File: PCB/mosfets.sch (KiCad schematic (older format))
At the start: 16 parts

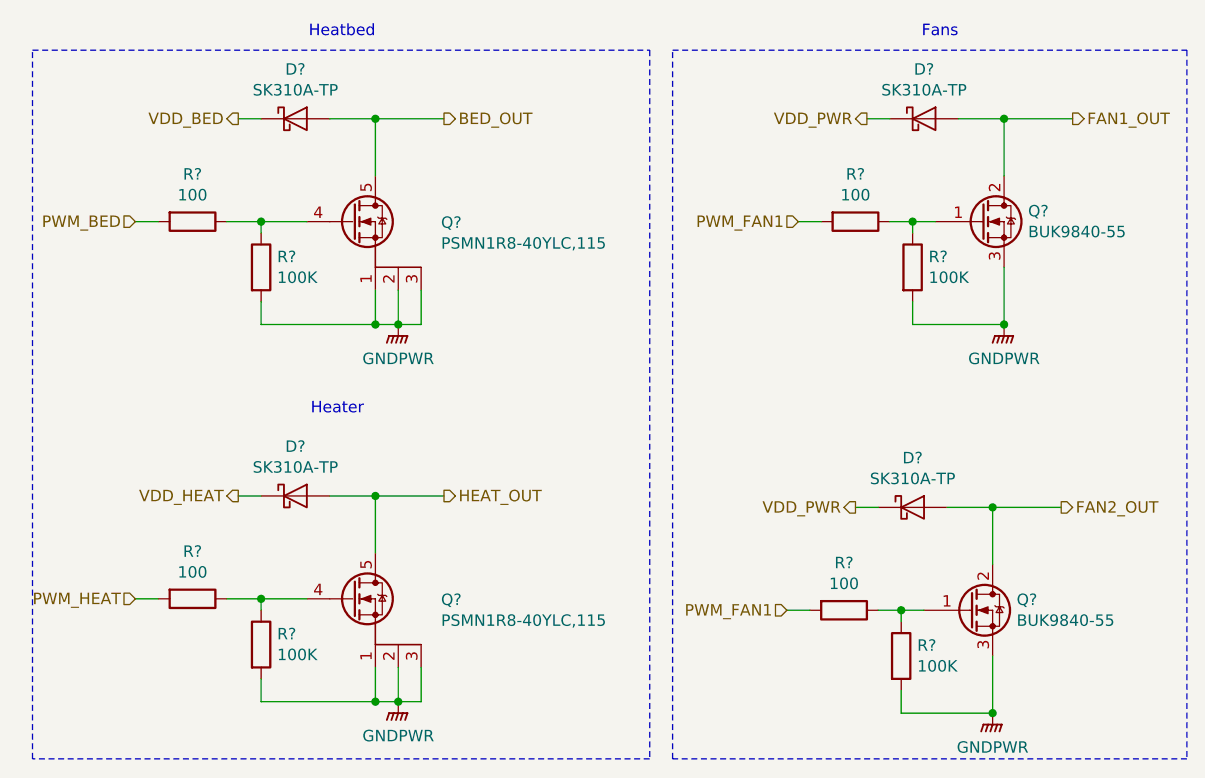
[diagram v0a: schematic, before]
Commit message: Removed some resistors for mosfets.
I don't think they are needed.
Also added some missing footprints.
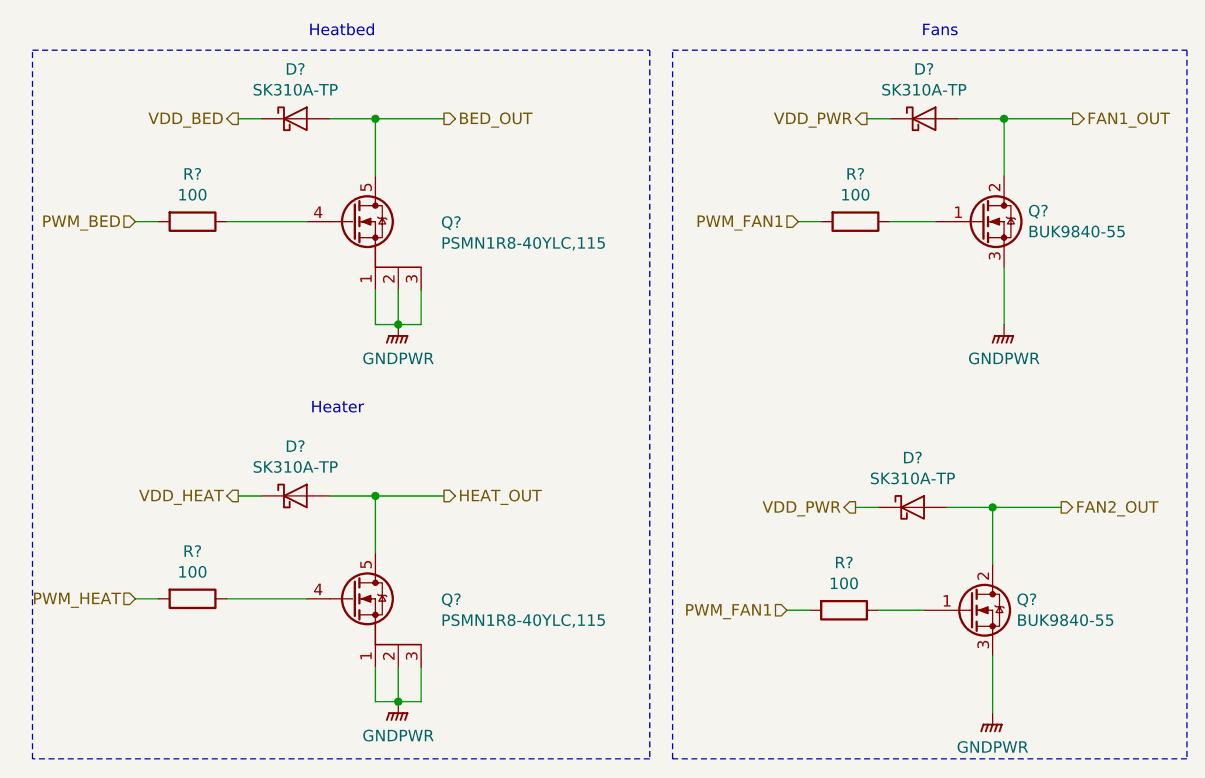
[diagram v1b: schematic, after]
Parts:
- removed R? (x4): 100K, Resistor_SMD:R_0603_1608Metric, symbol Device:R
- R? (x2): footprint (none) -> Resistor_SMD:R_0603_1608Metric
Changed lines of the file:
@@
 	2400 2600 2100 2600
 Connection ~ 2100 2600
-Wire Wire Line
-	1600 3050 1800 3050
-Wire Wire Line
-	1600 3100 1600 3050
-Connection ~ 1600 3050
-Wire Wire Line
-	1450 3050 1600 3050
-Wire Wire Line
-	1600 3400 1600 3500
-Connection ~ 2100 3500
-Wire Wire Line
-	1600 3500 2100 3500
-$Comp
-L Device:R R?
-U 1 1 5B1B03D2
-P 1600 3250
-F 0 "R?" H 1670 3296 50  0000 L CNN
-F 1 "100K" H 1670 3205 50  0000 L CNN
-F 2 "Resistor_SMD:R_0603_1608Metric" V 1530 3250 50  0001 C CNN
-F 3 "~" H 1600 3250 50  0001 C CNN
-	1    1600 3250
-	1    0    0    -1
-$EndComp
-Wire Wire Line
-	1600 1400 1800 1400
-Wire Wire Line
-	1450 1400 1600 1400
-Connection ~ 1600 1400
-Wire Wire Line
-	1600 1450 1600 1400
-Connection ~ 2100 1850
-Wire Wire Line
-	1600 1850 2100 1850
-Wire Wire Line
-	1600 1750 1600 1850
-$Comp
-L Device:R R?
-U 1 1 5B1A82F4
-P 1600 1600
-F 0 "R?" H 1670 1646 50  0000 L CNN
-F 1 "100K" H 1670 1555 50  0000 L CNN
-F 2 "Resistor_SMD:R_0603_1608Metric" V 1530 1600 50  0001 C CNN
-F 3 "~" H 1600 1600 50  0001 C CNN
-	1    1600 1600
-	1    0    0    -1
-$EndComp
 $Comp
 L remram-custom:BUK9840-55 Q?
@@
 F 0 "R?" V 3993 1400 50  0000 C CNN
 F 1 "100" V 4084 1400 50  0000 C CNN
-F 2 "" V 4130 1400 50  0001 C CNN
+F 2 "Resistor_SMD:R_0603_1608Metric" V 4130 1400 50  0001 C CNN
 F 3 "~" H 4200 1400 50  0001 C CNN
 	1    4200 1400
@@
 Wire Wire Line
 	3950 1400 4050 1400
-Wire Wire Line
-	4450 1750 4450 1850
-$Comp
-L Device:R R?
-U 1 1 5B1FCA24
-P 4450 1600
-F 0 "R?" H 4520 1646 50  0000 L CNN
-F 1 "100K" H 4520 1555 50  0000 L CNN
-F 2 "Resistor_SMD:R_0603_1608Metric" V 4380 1600 50  0001 C CNN
-F 3 "~" H 4450 1600 50  0001 C CNN
-	1    4450 1600
-	1    0    0    -1
-$EndComp
-Wire Wire Line
-	4350 1400 4450 1400
-Wire Wire Line
-	4450 1450 4450 1400
-Connection ~ 4450 1400
-Wire Wire Line
-	4450 1400 4550 1400
 $Comp
 L power:GNDPWR #PWR?
@@
 	1    0    0    -1
 $EndComp
-Wire Wire Line
-	4450 1850 4850 1850
-Connection ~ 4850 1850
 Text HLabel 5150 950  2    50   Output ~ 0
 FAN1_OUT
@@
 F 0 "R?" V 3943 3100 50  0000 C CNN
 F 1 "100" V 4034 3100 50  0000 C CNN
-F 2 "" V 4080 3100 50  0001 C CNN
+F 2 "Resistor_SMD:R_0603_1608Metric" V 4080 3100 50  0001 C CNN
 F 3 "~" H 4150 3100 50  0001 C CNN
 	1    4150 3100
@@
 Wire Wire Line
 	3900 3100 4000 3100
-Wire Wire Line
-	4400 3450 4400 3550
-$Comp
-L Device:R R?
-U 1 1 5B2008DA
-P 4400 3300
-F 0 "R?" H 4470 3346 50  0000 L CNN
-F 1 "100K" H 4470 3255 50  0000 L CNN
-F 2 "Resistor_SMD:R_0603_1608Metric" V 4330 3300 50  0001 C CNN
-F 3 "~" H 4400 3300 50  0001 C CNN
-	1    4400 3300
-	1    0    0    -1
-$EndComp
-Wire Wire Line
-	4300 3100 4400 3100
-Wire Wire Line
-	4400 3150 4400 3100
-Connection ~ 4400 3100
-Wire Wire Line
-	4400 3100 4500 3100
 $Comp
 L power:GNDPWR #PWR?
@@
 	1    0    0    -1
 $EndComp
-Wire Wire Line
-	4400 3550 4800 3550
-Connection ~ 4800 3550
 Text HLabel 5100 2650 2    50   Output ~ 0
 FAN2_OUT
@@
 Wire Notes Line
 	3400 650  5650 650
+Wire Wire Line
+	4350 1400 4550 1400
+Wire Wire Line
+	4300 3100 4500 3100
+Wire Wire Line
+	1450 1400 1800 1400
+Wire Wire Line
+	1450 3050 1800 3050
 $EndSCHEMATC

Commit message: Added PD registors on MOSFET gates.
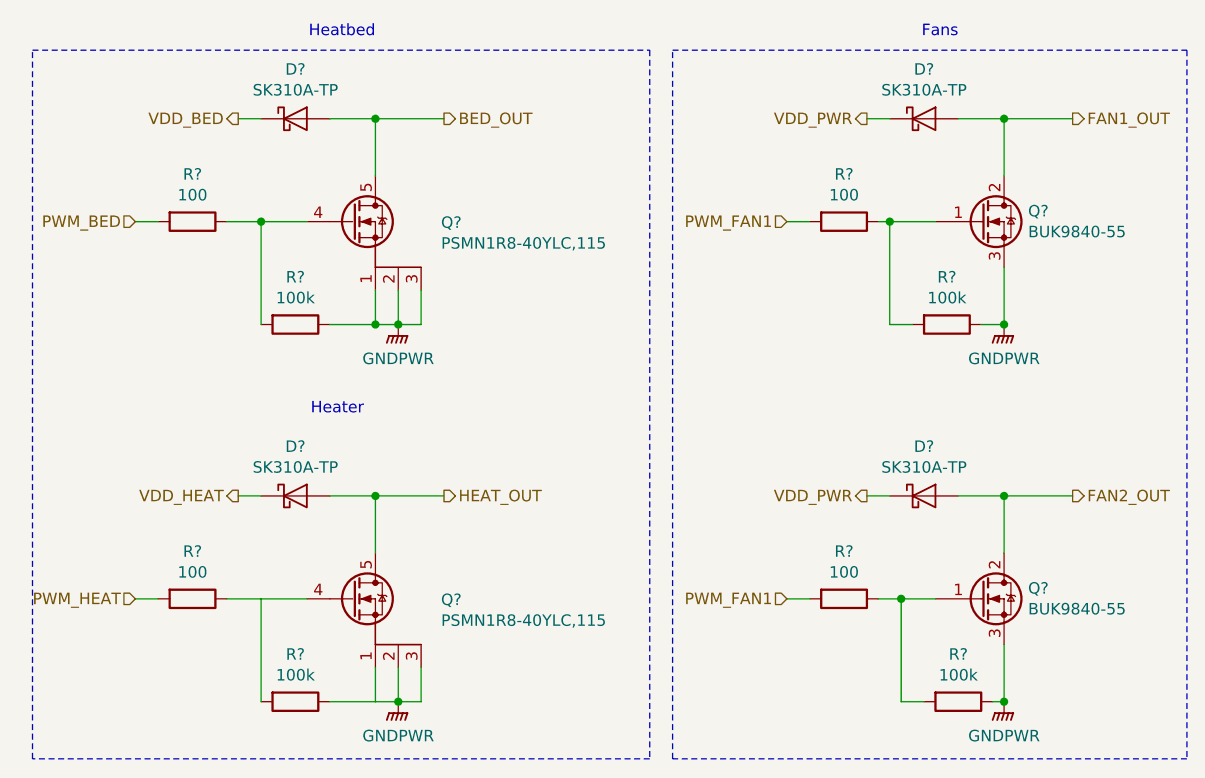
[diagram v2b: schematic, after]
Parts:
- added R? (x4): 100k, Resistor_SMD:R_0603_1608Metric, symbol Device:R
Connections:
- net GNDPWR: now also R?.1, R?.1, R?.1, R?.1
- net at Q?.4 (G), R?.1: now also R?.2
- net at Q?.1 (G), R?.1: now also R?.2 (x2)
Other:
- moved on the sheet: D?, Q?, R?
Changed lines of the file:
@@
 L Device:R R?
 U 1 1 5B1FB287
-P 4200 1400
-F 0 "R?" V 3993 1400 50  0000 C CNN
-F 1 "100" V 4084 1400 50  0000 C CNN
-F 2 "Resistor_SMD:R_0603_1608Metric" V 4130 1400 50  0001 C CNN
-F 3 "~" H 4200 1400 50  0001 C CNN
-	1    4200 1400
-	0    1    1    0
-$EndComp
-Text HLabel 3950 1400 0    50   Input ~ 0
+P 4150 1400
+F 0 "R?" V 3943 1400 50  0000 C CNN
+F 1 "100" V 4034 1400 50  0000 C CNN
+F 2 "Resistor_SMD:R_0603_1608Metric" V 4080 1400 50  0001 C CNN
+F 3 "~" H 4150 1400 50  0001 C CNN
+	1    4150 1400
+	0    1    1    0
+$EndComp
+Text HLabel 3900 1400 0    50   Input ~ 0
 PWM_FAN1
 Wire Wire Line
-	3950 1400 4050 1400
+	3900 1400 4000 1400
 $Comp
 L power:GNDPWR #PWR?
@@
 L remram-custom:BUK9840-55 Q?
 U 1 1 5B2008C9
-P 4700 3100
-F 0 "Q?" H 4905 3146 50  0000 L CNN
-F 1 "BUK9840-55" H 4905 3055 50  0000 L CNN
-F 2 "Package_TO_SOT_SMD:SOT-223-3_TabPin2" H 4900 3025 50  0001 L CIN
-F 3 "https://www.mouser.de/datasheet/2/916/BUK9840-55-1320170.pdf" H 4700 3100 50  0001 L CNN
-	1    4700 3100
+P 4750 3050
+F 0 "Q?" H 4955 3096 50  0000 L CNN
+F 1 "BUK9840-55" H 4955 3005 50  0000 L CNN
+F 2 "Package_TO_SOT_SMD:SOT-223-3_TabPin2" H 4950 2975 50  0001 L CIN
+F 3 "https://www.mouser.de/datasheet/2/916/BUK9840-55-1320170.pdf" H 4750 3050 50  0001 L CNN
+	1    4750 3050
 	1    0    0    -1
 $EndComp
@@
 L Device:R R?
 U 1 1 5B2008D0
-P 4150 3100
-F 0 "R?" V 3943 3100 50  0000 C CNN
-F 1 "100" V 4034 3100 50  0000 C CNN
-F 2 "Resistor_SMD:R_0603_1608Metric" V 4080 3100 50  0001 C CNN
-F 3 "~" H 4150 3100 50  0001 C CNN
-	1    4150 3100
-	0    1    1    0
-$EndComp
-Text HLabel 3900 3100 0    50   Input ~ 0
+P 4150 3050
+F 0 "R?" V 3943 3050 50  0000 C CNN
+F 1 "100" V 4034 3050 50  0000 C CNN
+F 2 "Resistor_SMD:R_0603_1608Metric" V 4080 3050 50  0001 C CNN
+F 3 "~" H 4150 3050 50  0001 C CNN
+	1    4150 3050
+	0    1    1    0
+$EndComp
+Text HLabel 3900 3050 0    50   Input ~ 0
 PWM_FAN1
 Wire Wire Line
-	3900 3100 4000 3100
+	3900 3050 4000 3050
 $Comp
 L power:GNDPWR #PWR?
 U 1 1 5B2008E5
-P 4800 3550
-F 0 "#PWR?" H 4800 3350 50  0001 C CNN
-F 1 "GNDPWR" H 4800 3400 50  0000 C CNN
-F 2 "" H 4800 3500 50  0001 C CNN
-F 3 "" H 4800 3500 50  0001 C CNN
-	1    4800 3550
-	1    0    0    -1
-$EndComp
-Text HLabel 5100 2650 2    50   Output ~ 0
+P 4850 3500
+F 0 "#PWR?" H 4850 3300 50  0001 C CNN
+F 1 "GNDPWR" H 4850 3350 50  0000 C CNN
+F 2 "" H 4850 3450 50  0001 C CNN
+F 3 "" H 4850 3450 50  0001 C CNN
+	1    4850 3500
+	1    0    0    -1
+$EndComp
+Text HLabel 5150 2600 2    50   Output ~ 0
 FAN2_OUT
-Text HLabel 4200 2650 0    50   Output ~ 0
+Text HLabel 4250 2600 0    50   Output ~ 0
 VDD_PWR
 $Comp
 L Device:D_Schottky D?
 U 1 1 5B2008EF
-P 4450 2650
-F 0 "D?" H 4450 2866 50  0000 C CNN
-F 1 "SK310A-TP" H 4450 2775 50  0000 C CNN
-F 2 "Diode_SMD:D_SMA" H 4450 2650 50  0001 C CNN
-F 3 "https://www.mouser.de/ProductDetail/Micro-Commercial-Components-MCC/SK310A-TP?qs=O2qRfqcg9D9SKx4%252bV6P4XQ%3D%3D" H 4450 2650 50  0001 C CNN
-	1    4450 2650
-	1    0    0    -1
-$EndComp
-Wire Wire Line
-	4200 2650 4300 2650
-Wire Wire Line
-	4800 2900 4800 2650
-Wire Wire Line
-	4600 2650 4800 2650
-Connection ~ 4800 2650
-Wire Wire Line
-	4800 2650 5100 2650
-Wire Wire Line
-	4800 3300 4800 3550
+P 4500 2600
+F 0 "D?" H 4500 2816 50  0000 C CNN
+F 1 "SK310A-TP" H 4500 2725 50  0000 C CNN
+F 2 "Diode_SMD:D_SMA" H 4500 2600 50  0001 C CNN
+F 3 "https://www.mouser.de/ProductDetail/Micro-Commercial-Components-MCC/SK310A-TP?qs=O2qRfqcg9D9SKx4%252bV6P4XQ%3D%3D" H 4500 2600 50  0001 C CNN
+	1    4500 2600
+	1    0    0    -1
+$EndComp
+Wire Wire Line
+	4250 2600 4350 2600
+Wire Wire Line
+	4850 2850 4850 2600
+Wire Wire Line
+	4650 2600 4850 2600
+Connection ~ 4850 2600
+Wire Wire Line
+	4850 2600 5150 2600
+Wire Wire Line
+	4850 3250 4850 3500
 Wire Notes Line
 	600  650  3300 650
@@
 	4350 1400 4550 1400
 Wire Wire Line
-	4300 3100 4500 3100
-Wire Wire Line
-	1450 1400 1800 1400
+	1450 1400 1600 1400
 Wire Wire Line
 	1450 3050 1800 3050
+$Comp
+L Device:R R?
+U 1 1 5AF82135
+P 1750 1850
+F 0 "R?" V 1543 1850 50  0000 C CNN
+F 1 "100k" V 1634 1850 50  0000 C CNN
+F 2 "Resistor_SMD:R_0603_1608Metric" V 1680 1850 50  0001 C CNN
+F 3 "~" H 1750 1850 50  0001 C CNN
+	1    1750 1850
+	0    1    1    0
+$EndComp
+Wire Wire Line
+	2100 1850 1900 1850
+Connection ~ 2100 1850
+Wire Wire Line
+	1600 1850 1600 1400
+Connection ~ 1600 1400
+Wire Wire Line
+	1600 1400 1800 1400
+$Comp
+L Device:R R?
+U 1 1 5AF8339E
+P 1750 3500
+F 0 "R?" V 1543 3500 50  0000 C CNN
+F 1 "100k" V 1634 3500 50  0000 C CNN
+F 2 "Resistor_SMD:R_0603_1608Metric" V 1680 3500 50  0001 C CNN
+F 3 "~" H 1750 3500 50  0001 C CNN
+	1    1750 3500
+	0    1    1    0
+$EndComp
+Wire Wire Line
+	2100 3500 1900 3500
+Wire Wire Line
+	1600 3500 1600 3050
+$Comp
+L Device:R R?
+U 1 1 5AF83BB4
+P 4600 1850
+F 0 "R?" V 4393 1850 50  0000 C CNN
+F 1 "100k" V 4484 1850 50  0000 C CNN
+F 2 "Resistor_SMD:R_0603_1608Metric" V 4530 1850 50  0001 C CNN
+F 3 "~" H 4600 1850 50  0001 C CNN
+	1    4600 1850
+	0    1    1    0
+$EndComp
+Wire Wire Line
+	4350 1850 4350 1400
+Wire Wire Line
+	4350 1850 4450 1850
+Wire Wire Line
+	4750 1850 4850 1850
+Connection ~ 4850 1850
+Wire Wire Line
+	4300 1400 4350 1400
+Connection ~ 4350 1400
+$Comp
+L Device:R R?
+U 1 1 5AF880C0
+P 4650 3500
+F 0 "R?" V 4443 3500 50  0000 C CNN
+F 1 "100k" V 4534 3500 50  0000 C CNN
+F 2 "Resistor_SMD:R_0603_1608Metric" V 4580 3500 50  0001 C CNN
+F 3 "~" H 4650 3500 50  0001 C CNN
+	1    4650 3500
+	0    1    1    0
+$EndComp
+Wire Wire Line
+	4400 3500 4400 3050
+Wire Wire Line
+	4400 3500 4500 3500
+Wire Wire Line
+	4300 3050 4400 3050
+Connection ~ 4400 3050
+Wire Wire Line
+	4400 3050 4550 3050
+Wire Wire Line
+	4850 3500 4800 3500
+Connection ~ 4850 3500
 $EndSCHEMATC

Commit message: Changed some sheets and added LICENCE.
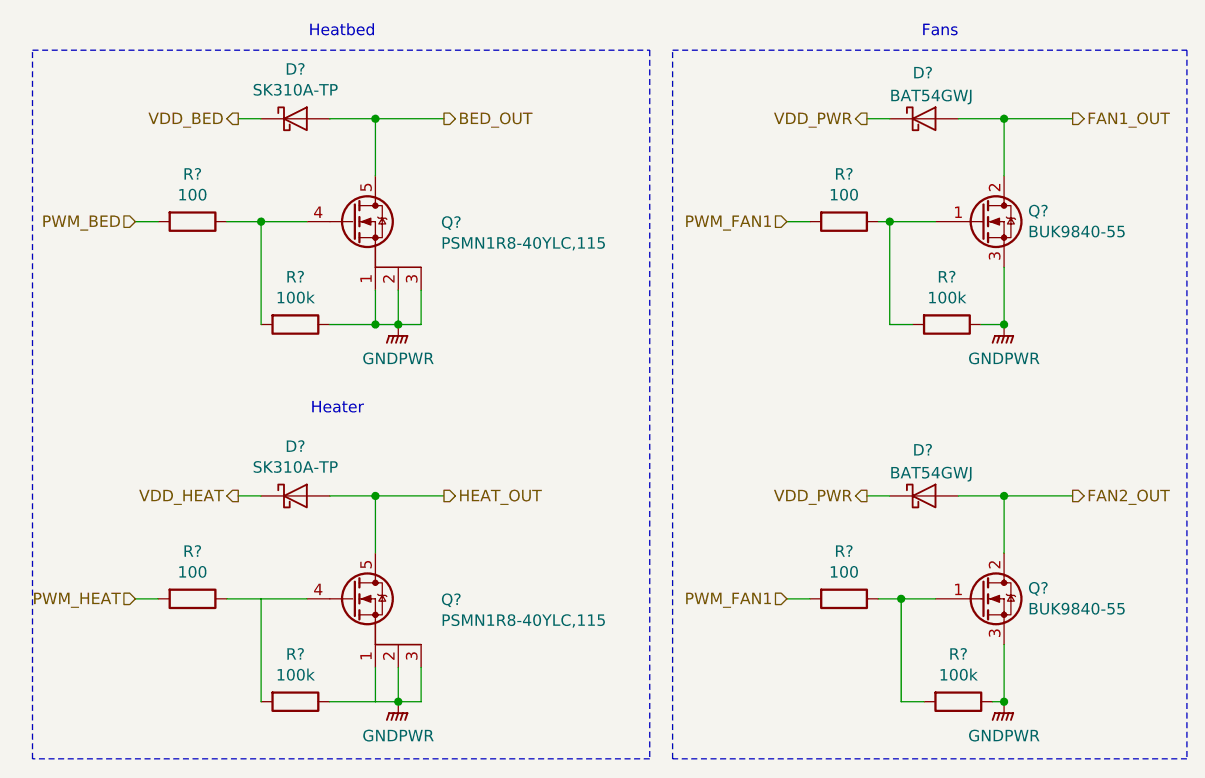
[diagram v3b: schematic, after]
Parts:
- removed D? (x2): SK310A-TP, Diode_SMD:D_SMA, symbol Device:D_Schottky
- added D? (x2): BAT54GWJ, Diode_SMD:D_SOD-123, symbol Device:D_Schottky
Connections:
- net FAN1_OUT: now also D?.2 (A)
- net FAN2_OUT: now also D?.2 (A)
- net VDD_PWR: now also D?.1 (K), D?.1 (K)
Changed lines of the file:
@@
 Text HLabel 4250 950  0    50   Output ~ 0
 VDD_PWR
-$Comp
-L Device:D_Schottky D?
-U 1 1 5B1FEED7
-P 4500 950
-F 0 "D?" H 4500 1166 50  0000 C CNN
-F 1 "SK310A-TP" H 4500 1075 50  0000 C CNN
-F 2 "Diode_SMD:D_SMA" H 4500 950 50  0001 C CNN
-F 3 "https://www.mouser.de/ProductDetail/Micro-Commercial-Components-MCC/SK310A-TP?qs=O2qRfqcg9D9SKx4%252bV6P4XQ%3D%3D" H 4500 950 50  0001 C CNN
-	1    4500 950
-	1    0    0    -1
-$EndComp
 Wire Wire Line
 	4250 950  4350 950
@@
 Text HLabel 4250 2600 0    50   Output ~ 0
 VDD_PWR
-$Comp
-L Device:D_Schottky D?
-U 1 1 5B2008EF
-P 4500 2600
-F 0 "D?" H 4500 2816 50  0000 C CNN
-F 1 "SK310A-TP" H 4500 2725 50  0000 C CNN
-F 2 "Diode_SMD:D_SMA" H 4500 2600 50  0001 C CNN
-F 3 "https://www.mouser.de/ProductDetail/Micro-Commercial-Components-MCC/SK310A-TP?qs=O2qRfqcg9D9SKx4%252bV6P4XQ%3D%3D" H 4500 2600 50  0001 C CNN
-	1    4500 2600
-	1    0    0    -1
-$EndComp
 Wire Wire Line
 	4250 2600 4350 2600
@@
 	4850 3500 4800 3500
 Connection ~ 4850 3500
+$Comp
+L Device:D_Schottky D?
+U 1 1 5AFB8598
+P 4500 950
+F 0 "D?" H 4450 1150 50  0000 L CNN
+F 1 "BAT54GWJ" H 4350 1050 50  0000 L CNN
+F 2 "Diode_SMD:D_SOD-123" H 4500 950 50  0001 C CNN
+F 3 "https://www.mouser.de/datasheet/2/916/BAT54GW-1318921.pdf" H 4500 950 50  0001 C CNN
+	1    4500 950
+	1    0    0    -1
+$EndComp
+$Comp
+L Device:D_Schottky D?
+U 1 1 5AFBAFD7
+P 4500 2600
+F 0 "D?" H 4450 2800 50  0000 L CNN
+F 1 "BAT54GWJ" H 4350 2700 50  0000 L CNN
+F 2 "Diode_SMD:D_SOD-123" H 4500 2600 50  0001 C CNN
+F 3 "https://www.mouser.de/datasheet/2/916/BAT54GW-1318921.pdf" H 4500 2600 50  0001 C CNN
+	1    4500 2600
+	1    0    0    -1
+$EndComp
 $EndSCHEMATC

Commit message: Finished first draft of the schematics.
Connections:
- net PWM_FAN1: no longer R?.2
- new net PWM_FAN2: R?.2
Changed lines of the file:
@@
 $Descr A4 11693 8268
 encoding utf-8
-Sheet 5 5
+Sheet 5 9
 Title "MOSFET"
 Date ""
@@
 $EndComp
 Text HLabel 3900 3050 0    50   Input ~ 0
-PWM_FAN1
+PWM_FAN2
 Wire Wire Line
 	3900 3050 4000 3050
